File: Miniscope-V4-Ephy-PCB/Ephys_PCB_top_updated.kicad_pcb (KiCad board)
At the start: 2 copper layers, 44 parts, among them J1 34 Circuit Slimslack Connector, J10 Conn_01x01, J11 Conn_01x01, J12 Conn_01x01, J13 Conn_01x01, J4 Conn_01x01, J5 Conn_01x01, J6 Conn_01x01, J7 , J8 Conn_01x01, J9 Conn_01x01, U1 ATSAMS70N21A-CFNT, U2 RHD2132_QFN-RHD2132, U3 ABM8G-12.000MHZ-4Y-T3, U4 TXB0304RUT, U5 LTST-C191KRKT, U6 TLV7103318DSER

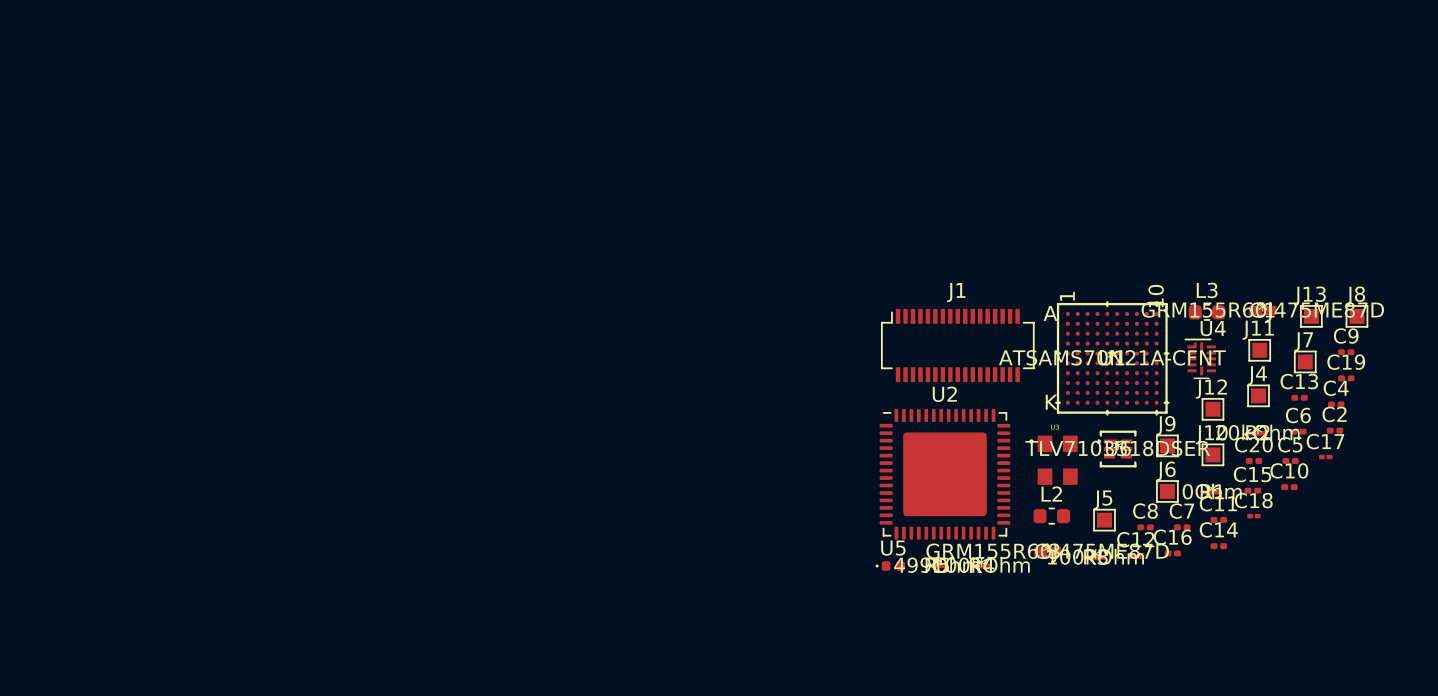
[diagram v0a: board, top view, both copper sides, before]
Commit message: Update schematic and footprints
* Replaced MCU symbol, pinout, and footprint with correct one (TFBGA version).
* Created and replaced slimstack connector with the correct one.
* Replaced crystal oscillator with better symbol
* Tried to link as many footprints as possible to those contained in the Aharoni KiCad Library.
* TODO: Add transistor to drive status LED.
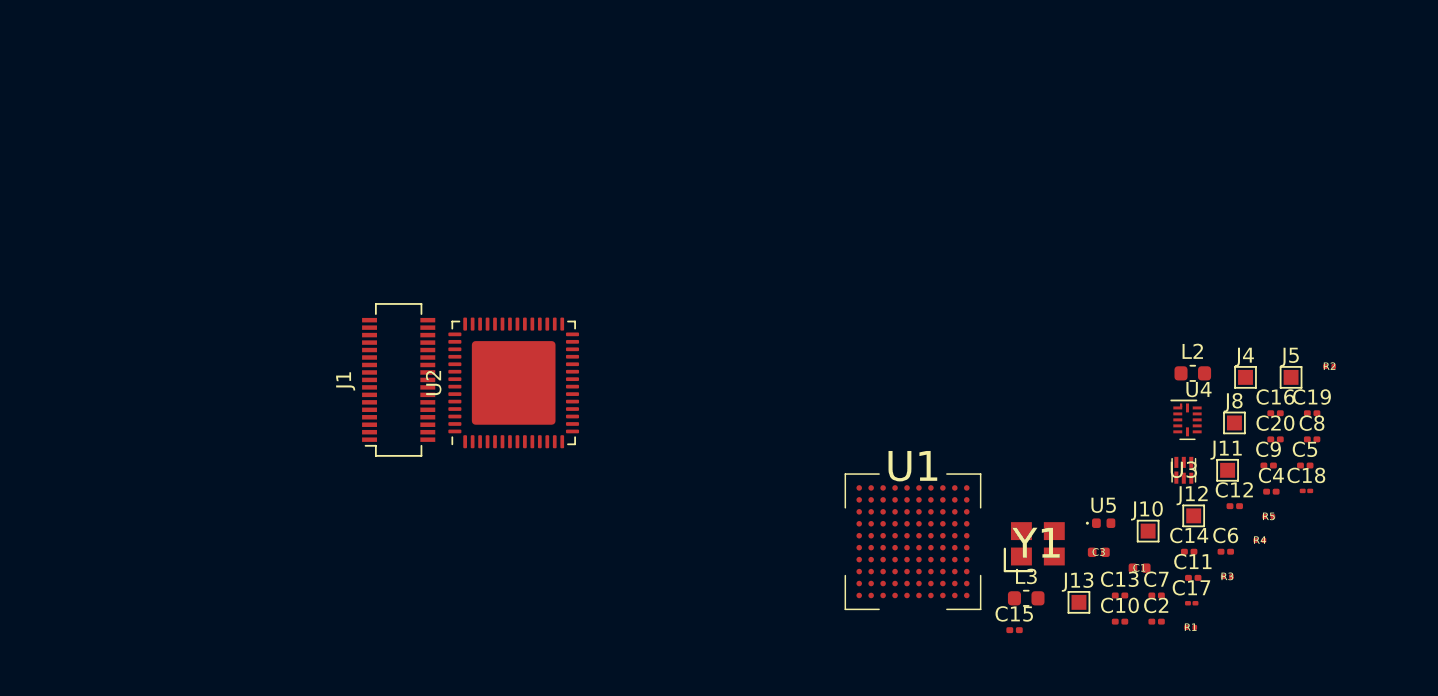
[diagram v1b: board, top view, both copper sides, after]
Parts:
- removed J6, J9: Conn_01x01, TestPoint:TestPoint_Pad_1.0x1.0mm
- removed J7: , TestPoint:TestPoint_Pad_1.0x1.0mm
- removed U6: TLV7103318DSER, TLV7103318DSER_ldo:TLV7103318DSER
- added Y1: ABM8G-12.000MHZ-4Y-T3, .Oscillator:OSCCC320X250X100L80X100, F.Cu at (155.4, 103.4)
- C1, C3: value GRM155R60J475ME87D -> 4.7uF; footprint cap_GRM155R60J475ME47D:GRM155R60J475ME47D -> .Capacitor:C_0402_1005Metric_L
- R1: value 0Ohm -> 0; footprint res_ERJ1GEF1003C:ERJ-1GEF1003C -> .Resistor:R_0201_0603Metric_ERJ_L
- R2: value 20kOhm -> 20K; footprint res_ERJ1GEF2002C:ERJ-1GEF2002C -> .Resistor:R_0201_0603Metric_ERJ_L
- R3, R4: value 100kOhm -> 100K; footprint res_ERJ1GEF1003C:ERJ-1GEF1003C -> .Resistor:R_0201_0603Metric_ERJ_L
- R5: value 499Ohm -> 499; footprint res_ERJ1GEF1003C:ERJ-1GEF1003C -> .Resistor:R_0201_0603Metric_ERJ_L
- U1: value ATSAMS70N21A-CFNT -> ATSAME70N21A-CN; footprint ATSAMS70N21ACFNT:ATSAMS70N21A-CFNT -> .Package_BGA:BGA_100_CP80_10X10_900X900X110B40L
- U3: value ABM8G-12.000MHZ-4Y-T3 -> TLV7103318DSER; footprint ABM8G-12:OSCSC320X250X100N -> .Package_SON:SON_6_P50_150X150X80L50X25L
- moved J1 37.5 mm to (112.6, 92.4), turned to 90 degrees
- moved U2 29.5 mm to (120.3, 92.6), turned to 90 degrees
- moved J13 24.7 mm to (158.1, 107.3)
- moved L3 22.6 mm to (154.6, 107.0)
- moved R5 22.4 mm to (170.8, 101.5)
- moved C1 19.1 mm to (162.2, 105.0)
- moved R4 18.7 mm to (170.2, 103.1)
- moved C15 18.5 mm to (153.8, 109.2)
- moved U1 18.1 mm to (147.0, 103.2)
- moved C13 17.9 mm to (160.9, 106.8)
- moved C2 17.5 mm to (163.3, 108.6)
- moved J5 15.7 mm to (172.3, 92.2)
- moved C10 14.5 mm to (160.9, 108.6)
- moved U5 14.4 mm to (159.8, 102.0)
- moved L2 13.4 mm to (165.8, 92.0)
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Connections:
- net /VDDMIC renamed /VDDUTMIC
- C10 pad 1: +1V8 -> /VDDCORE
- C11 pad 1: +3V3 -> +5V
- C12 pad 1: +1V8 -> /VDDCORE
- C13 pad 2: GND -> Net-(C13-Pad2)
- C17 pad 1: GND -> Net-(C17-Pad1)
- C19 pad 2: Net-(C19-Pad2) -> Net-(C13-Pad2)
- C8 pad 1: +1V8 -> /VDDCORE
- C9 pad 1: +1V8 -> /VDDCORE
- J1 pad 1: /REF_ELEC -> /IN7
- J1 pad 10: /IN16 -> /IN12
- J1 pad 11: /IN17 -> /IN2
- J1 pad 12: /IN18 -> /IN13
- J1 pad 13: /IN19 -> /IN1
- J1 pad 14: /IN20 -> /IN14
- J1 pad 15: /IN21 -> /IN0
- J1 pad 16: /IN22 -> /IN15
- J1 pad 17: /IN23 -> /IN31
- J1 pad 18: /IN24 -> /IN16
- J1 pad 19: /IN25 -> /IN30
- J1 pad 20: /IN26 -> /IN17
- J1 pad 21: /IN27 -> /IN29
- J1 pad 22: /IN28 -> /IN18
- J1 pad 23: /IN29 -> /IN28
- J1 pad 24: /IN30 -> /IN19
- J1 pad 25: /IN31 -> /IN27
- J1 pad 26: /IN0 -> /IN20
- J1 pad 27: /IN1 -> /IN26
- J1 pad 28: /IN2 -> /IN21
- J1 pad 29: /IN3 -> /IN25
- J1 pad 3: /IN9 -> /IN6
- J1 pad 30: /IN4 -> /IN22
- J1 pad 31: /IN5 -> /IN24
- J1 pad 32: /IN6 -> /IN23
- J1 pad 33: /IN7 -> /REF_ELEC
- J1 pad 4: /IN10 -> /IN9
- J1 pad 5: /IN11 -> /IN5
- J1 pad 6: /IN12 -> /IN10
- J1 pad 7: /IN13 -> /IN4
- J1 pad 8: /IN14 -> /IN11
- J1 pad 9: /IN15 -> /IN3
- J13 pad 1: +3V3 -> +5V
- L2 pad 1: +1V8 -> /VDDCORE
- L3 pad 1: +1V8 -> /VDDCORE
- R1 pad 1: /REF_ELEC -> GND
- R1 pad 2: GND -> /REF_ELEC
- R2 pad 1: +3V3 -> GND
- R2 pad 2: GND -> +3V3
- U1 pad A6: GND -> Net-(U1-PadA6)
- U1 pad A8: Net-(U1-PadA8) -> GND
- U1 pad B1: /LINEVALID -> Net-(U1-PadB1)
- U1 pad C3: +1V8 -> /VDDCORE
- U1 pad C6: +1V8 -> /VDDCORE
- U1 pad D2: GND -> Net-(U1-PadD2)
- U1 pad D3: Net-(U1-PadD3) -> GND
- U1 pad D6: +1V8 -> /VDDCORE
- U1 pad D7: Net-(U1-PadD7) -> /VDDPLL
- U1 pad E4: +1V8 -> GND
- U1 pad E6: GND -> +1V8
- U1 pad G6: +1V8 -> /VDDCORE
- U1 pad H1: /SPI1_NPCS0 -> /SPI0_NPCS0
- U3 pad 1: GND -> +5V
- U3 pad 2: GND -> +5V
- U3 pad 3: Net-(C18-Pad1) -> Net-(U3-Pad3)

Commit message: Group components in PCB layout
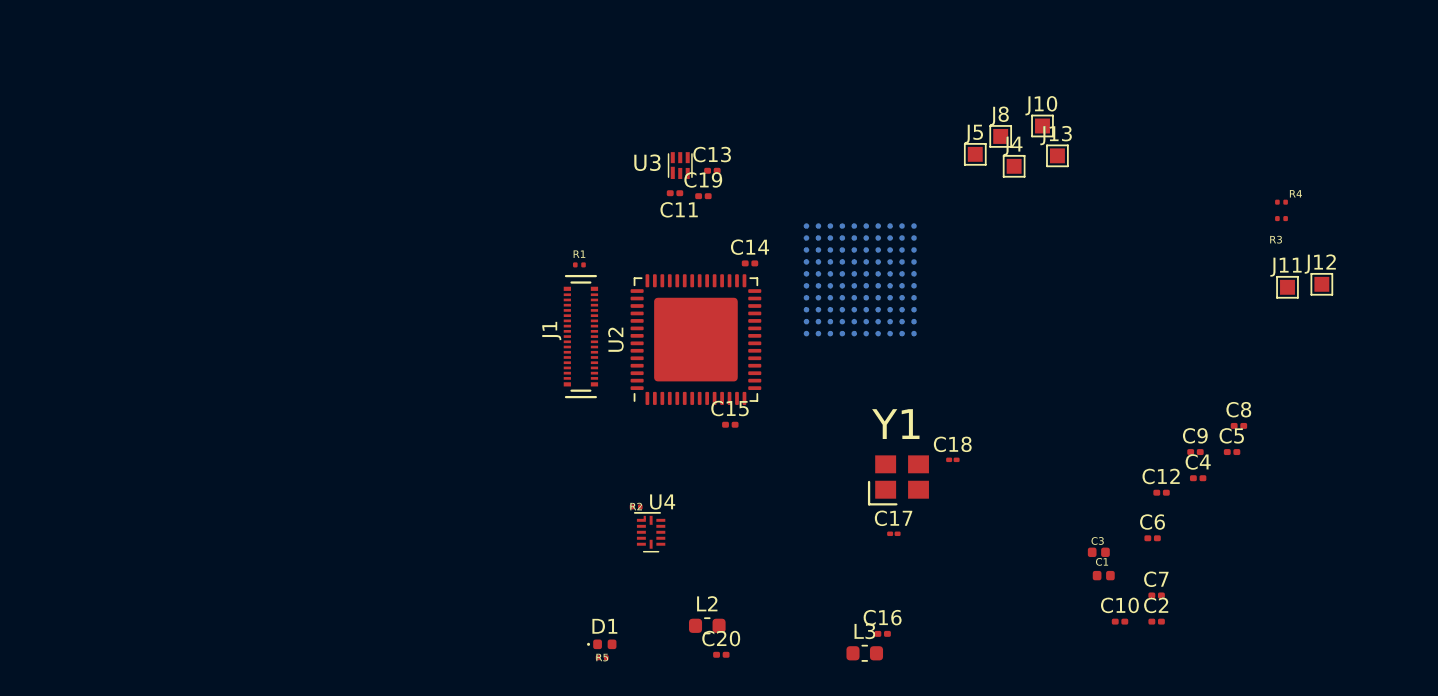
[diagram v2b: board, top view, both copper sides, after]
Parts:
- removed U5: LTST-C191KRKT, LED_SMD:LED_0402_1005Metric
- added D1: LED_Small_ALT, LED_SMD:LED_0402_1005Metric, F.Cu at (126.4, 110.1)
- J1: footprint Connector_Molex:Molex_SlimStack_55560-0341_2x17_P0.50mm_Vertical -> .Connector:SS_5046223412
- U1: moved to B.Cu
- moved R1 47.6 mm to (124.7, 84.7)
- moved R2 47.4 mm to (128.5, 100.9)
- moved R5 45.6 mm to (126.2, 111.0)
- moved C19 43.3 mm to (133.0, 80.1)
- moved C11 43.2 mm to (131.1, 79.9)
- moved C20 39.8 mm to (134.2, 110.8)
- moved C13 39.4 mm to (133.6, 78.4)
- moved U3 39.4 mm to (131.4, 78.0)
- moved U4 36.7 mm to (129.5, 102.6)
- moved L2 36.6 mm to (133.3, 108.9)
- moved C14 35.2 mm to (136.1, 84.6)
- moved C16 30.2 mm to (145.0, 109.4)
- moved J13 29.9 mm to (156.7, 77.4)
- moved J10 28.0 mm to (155.7, 75.4)
- moved J5 25.9 mm to (151.2, 77.3)
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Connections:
- J1 pad 1: /IN7 -> /IN8
- J1 pad 10: /IN12 -> /IN17
- J1 pad 11: /IN2 -> /IN18
- J1 pad 12: /IN13 -> /IN19
- J1 pad 13: /IN1 -> /IN20
- J1 pad 14: /IN14 -> /IN21
- J1 pad 15: /IN0 -> /IN22
- J1 pad 16: /IN15 -> /IN23
- J1 pad 17: /IN31 -> GND
- J1 pad 18: /IN16 -> /REF_ELEC
- J1 pad 19: /IN30 -> /IN24
- J1 pad 2: /IN8 -> /IN9
- J1 pad 20: /IN17 -> /IN25
- J1 pad 21: /IN29 -> /IN26
- J1 pad 22: /IN18 -> /IN27
- J1 pad 24: /IN19 -> /IN29
- J1 pad 25: /IN27 -> /IN30
- J1 pad 26: /IN20 -> /IN31
- J1 pad 27: /IN26 -> /IN0
- J1 pad 28: /IN21 -> /IN1
- J1 pad 29: /IN25 -> /IN2
- J1 pad 3: /IN6 -> /IN10
- J1 pad 30: /IN22 -> /IN3
- J1 pad 31: /IN24 -> /IN4
- J1 pad 32: /IN23 -> /IN5
- J1 pad 33: /REF_ELEC -> /IN6
- J1 pad 34: GND -> /IN7
- J1 pad 4: /IN9 -> /IN11
- J1 pad 5: /IN5 -> /IN12
- J1 pad 6: /IN10 -> /IN13
- J1 pad 7: /IN4 -> /IN14
- J1 pad 8: /IN11 -> /IN15
- J1 pad 9: /IN3 -> /IN16
- R1 pad 1: GND -> /REF_ELEC
- R1 pad 2: /REF_ELEC -> GND
- R5 pad 1: /RED_LED -> Net-(D1-Pad1)
